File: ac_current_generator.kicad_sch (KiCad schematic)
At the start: 29 parts, among them U1 AD8066ARZ-RL, U2 AD8066ARZ-RL, U3 AD8065ART-R2

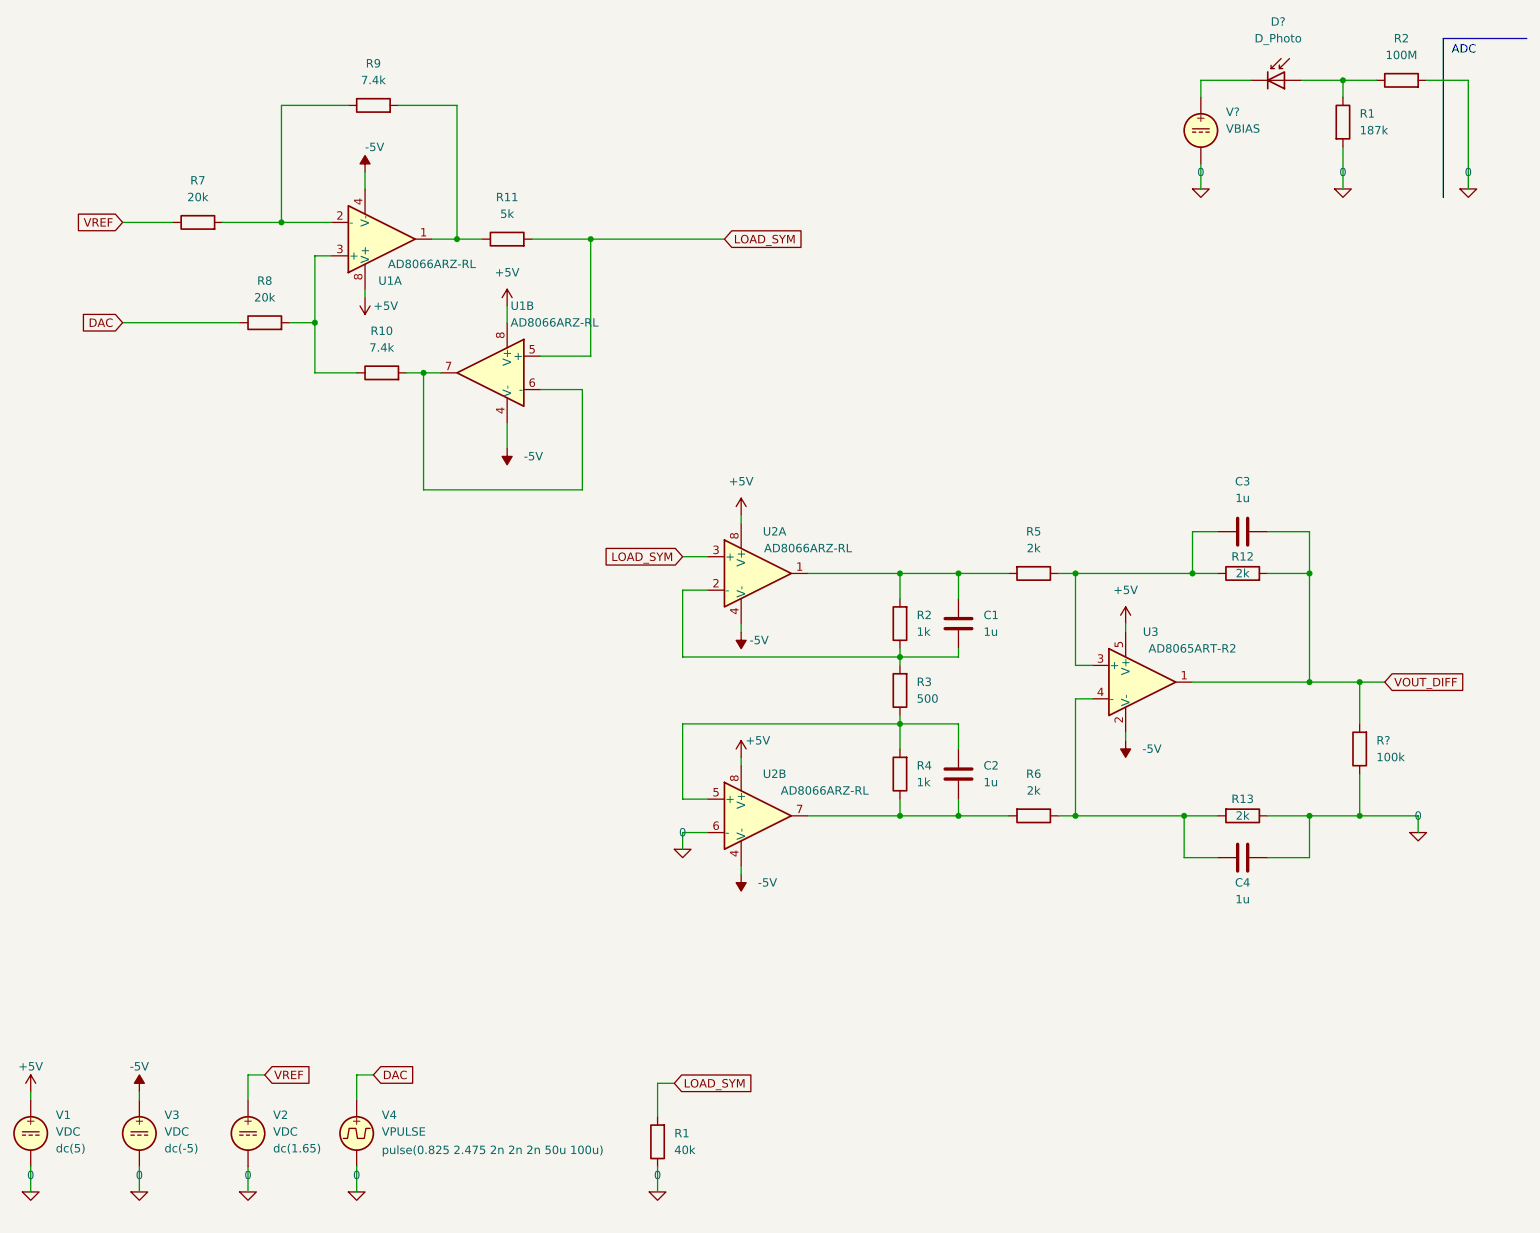
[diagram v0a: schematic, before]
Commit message: relative path to library added
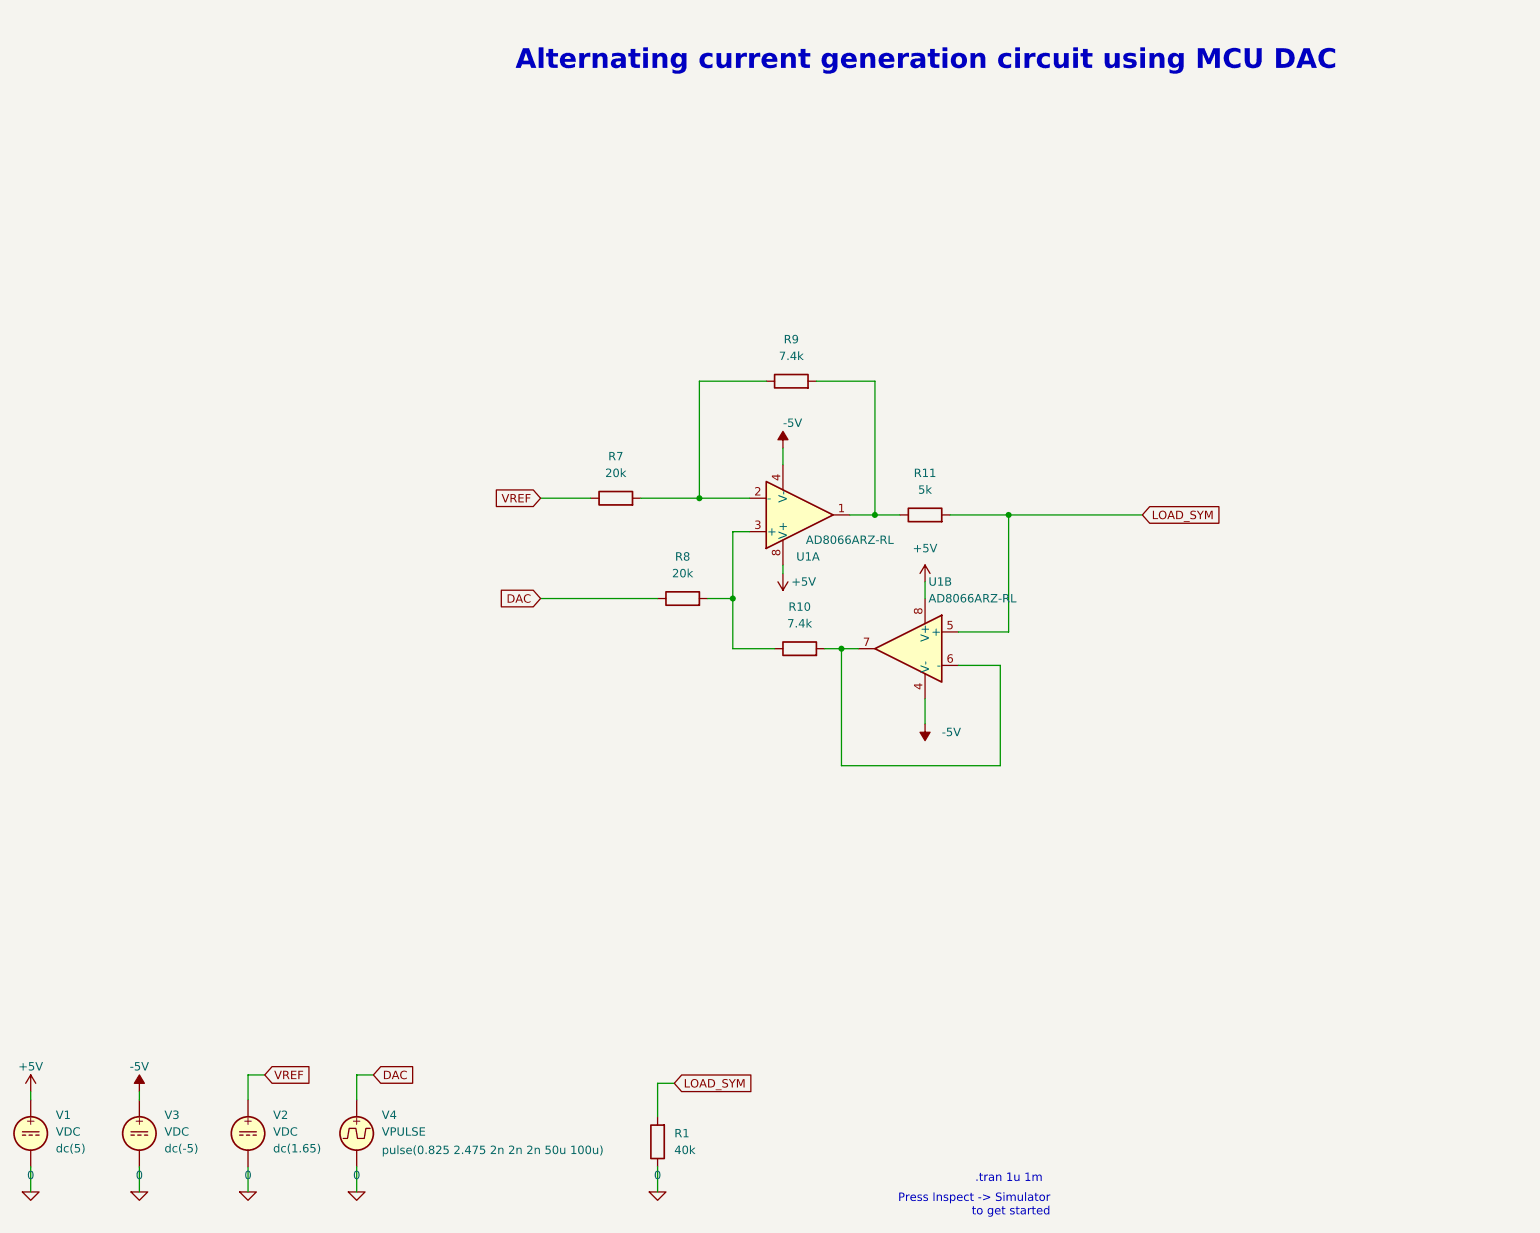
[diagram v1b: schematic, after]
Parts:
- removed C1, C2, C3, C4: 1u, symbol Device:C
- removed D?: D_Photo, symbol Device:D_Photo
- removed R1: 187k, symbol Device:R
- removed R12, R13, R5, R6: 2k, Resistor_SMD:R_0603_1608Metric, symbol Device:R
- removed R2: 100M, symbol Device:R
- removed R2, R4: 1k, Resistor_SMD:R_0603_1608Metric, symbol Device:R
- removed R3: 500, Resistor_SMD:R_0603_1608Metric, symbol Device:R
- removed R?: 100k, Resistor_SMD:R_0603_1608Metric, symbol Device:R
- removed U2: AD8066ARZ-RL, Project_PCB_library:SOIC127P599X175-8N, symbol Project_lib:AD8066ARZ-RL
- removed U3: AD8065ART-R2, Project_PCB_library:SOT-23-5_HandSoldering, symbol Project_lib:AD8065ART-R2
- removed V?: VBIAS, symbol Simulation_SPICE:VDC
- U1: Spice_Lib_File C:\Users\denis\Documents\GitHub\AC_voltage_gen_with_current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 -> Libraries\SPICE_models\AD8066-dual.lib
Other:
- note added: ".tran 1u 1m"
- note added: "Alternating current generation circuit using MCU DAC"
- note added: "Press Inspect -> Simulator to get started"
- note removed: "ADC"
- title: (none) -> AC current generator
- moved on the sheet: R10, R11, R7, R8, R9, U1A, U1B
